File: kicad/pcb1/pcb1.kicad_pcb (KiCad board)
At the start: 2 copper layers, 42.5 x 54 mm, 5 parts, among them J1 Conn_01x12_Pin, SW1 SW_Push

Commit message: BOM aufgenommen
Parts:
- moved SW1 42.1 mm to (100.4, 115.0)
- moved R1 41.1 mm to (100.0, 110.5), turned to 0 degrees
- moved J1 19.8 mm to (105.5, 87.1)
- moved C1 19.6 mm to (100.5, 73.5)
- moved A1 18.6 mm to (69.8, 75.8)
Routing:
- net Net-(A1-ADC1_CH6/D34): track 53.0 -> 18.8 mm
- net 3V3: track 58.3 -> 47.9 mm, vias 1 -> 0
- net Net-(A1-VIN): track 13.6 -> 6.27 mm
- net D26: track 29.8 -> 23.2 mm
- net D25: track 21.4 -> 16.0 mm, vias 1 -> 0
- net D27: track 32.4 -> 27.6 mm
- net GND: track 3.03 -> 1.53 mm, vias 2 -> 1
- net D23: track 44.8 -> 43.6 mm
- net D17: track 38.2 -> 37.0 mm
- net D16: track 38.2 -> 37.0 mm
- net D22: track 41.4 -> 40.2 mm
- net D21: track 39.3 -> 38.1 mm
- net D19: track 39.3 -> 38.1 mm
- net D18: track 39.3 -> 38.1 mm
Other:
- board size 42.5 x 54 mm -> 42.5 x 53.5 mm
- board text added: "Blinklicht-Device - Thilo Berger 2026 for ESP32DevkitV1 - PCB: v1"

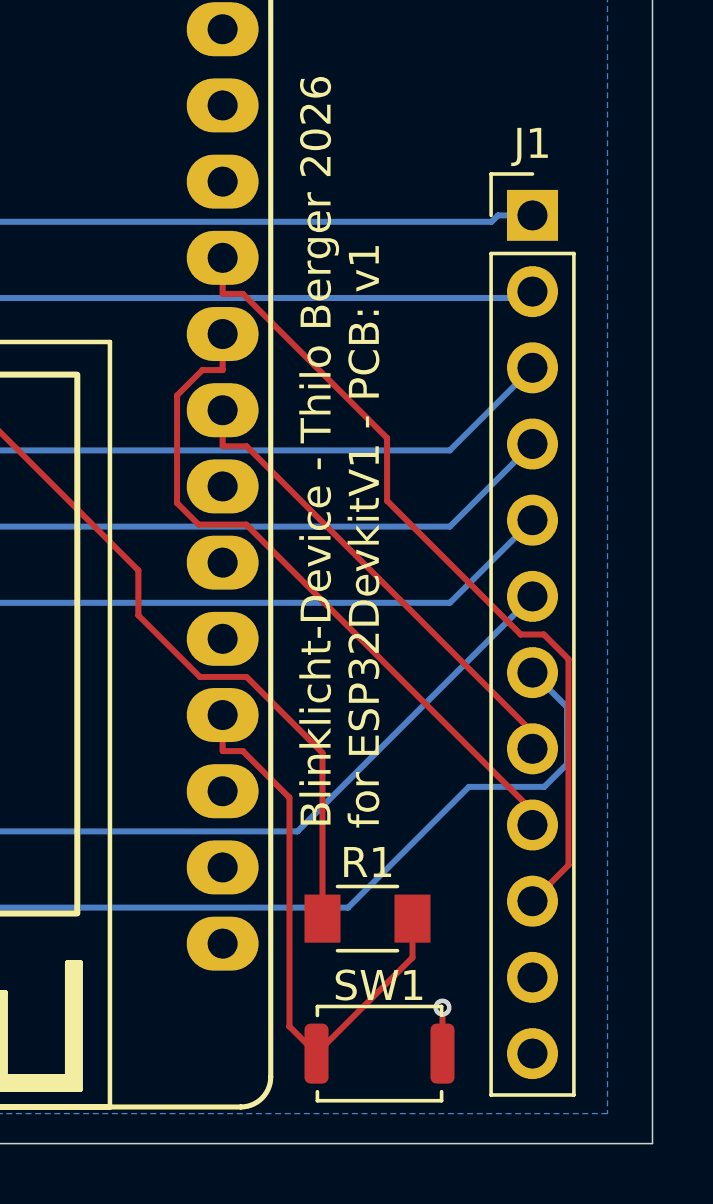
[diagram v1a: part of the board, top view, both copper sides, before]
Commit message: added Pin Desc
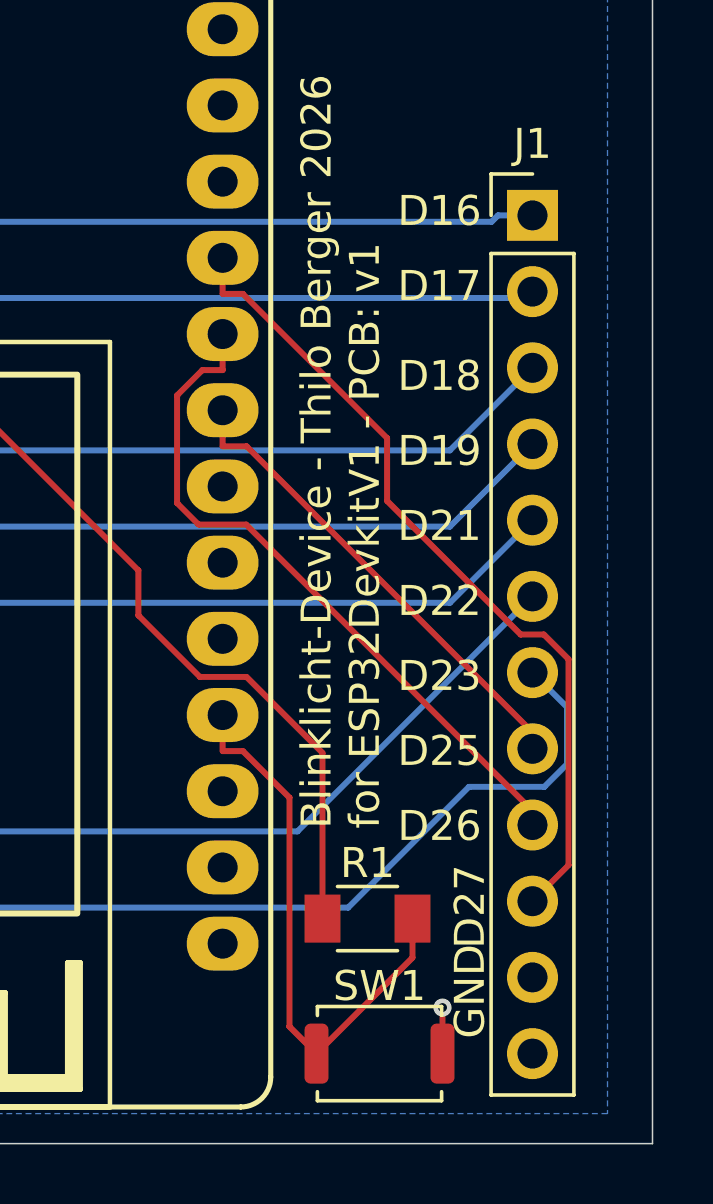
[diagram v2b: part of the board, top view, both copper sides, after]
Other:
- board text added: "D16"
- board text added: "D17"
- board text added: "D18"
- board text added: "D19"
- board text added: "D21"
- board text added: "D22"
- board text added: "D23"
- board text added: "D25"
- board text added: "D26"
- board text added: "D27"
- board text added: "GND"
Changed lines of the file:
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@@
+		)
+	)
+	(gr_text "D16"
+		(at 101 87.5 0)
+		(layer "F.SilkS")
+		(effects
+			(font
+				(size 1 1)
+				(thickness 0.1)
+			)
+			(justify left bottom)
+		)
+	)
+	(gr_text "D17"
+		(at 101 90 0)
+		(layer "F.SilkS")
+		(effects
+			(font
+				(size 1 1)
+				(thickness 0.1)
+			)
+			(justify left bottom)
+		)
+	)
+	(gr_text "D18"
+		(at 101 93 0)
+		(layer "F.SilkS")
+		(effects
+			(font
+				(size 1 1)
+				(thickness 0.1)
+			)
+			(justify left bottom)
+		)
+	)
+	(gr_text "D19"
+		(at 101 95.5 0)
+		(layer "F.SilkS")
+		(effects
+			(font
+				(size 1 1)
+				(thickness 0.1)
+			)
+			(justify left bottom)
+		)
+	)
+	(gr_text "D21"
+		(at 101 98 0)
+		(layer "F.SilkS")
+		(effects
+			(font
+				(size 1 1)
+				(thickness 0.1)
+			)
+			(justify left bottom)
+		)
+	)
+	(gr_text "D22"
+		(at 101 100.5 0)
+		(layer "F.SilkS")
+		(effects
+			(font
+				(size 1 1)
+				(thickness 0.1)
+			)
+			(justify left bottom)
+		)
+	)
+	(gr_text "D23"
+		(at 101 103 0)
+		(layer "F.SilkS")
+		(effects
+			(font
+				(size 1 1)
+				(thickness 0.1)
+			)
+			(justify left bottom)
+		)
+	)
+	(gr_text "D25"
+		(at 101 105.5 0)
+		(layer "F.SilkS")
+		(effects
+			(font
+				(size 1 1)
+				(thickness 0.1)
+			)
+			(justify left bottom)
+		)
+	)
+	(gr_text "D26"
+		(at 101 108 0)
+		(layer "F.SilkS")
+		(effects
+			(font
+				(size 1 1)
+				(thickness 0.1)
+			)
+			(justify left bottom)
+		)
+	)
+	(gr_text "D27"
+		(at 104 111.5 90)
+		(layer "F.SilkS")
+		(effects
+			(font
+				(size 1 1)
+				(thickness 0.1)
+			)
+			(justify left bottom)
+		)
+	)
+	(gr_text "GND"
+		(at 104 114.5 90)
+		(layer "F.SilkS")
+		(effects
+			(font
+				(size 1 1)
+				(thickness 0.1)
+			)
+			(justify left bottom)
 		)
 	)
